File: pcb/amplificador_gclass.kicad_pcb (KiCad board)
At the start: 2 copper layers, 199.5 x 70.5 mm, 97 parts, among them CON1 AUDIO_IN, P1 +VA_GND, P10 2SC3281, P11 2SC3281, P12 2SA1302, P13 CONN_01X01, P14 CONN_01X01, P15 CONN_01X01, P16 CONN_01X01, P17 CONN_01X01, P18 CONN_01X01, P2 +VB_GND, P3 -VA_GND, P4 -VB_GND, P5 OUT, P6 CONN_01X01, P7 MJE350, P8 MJE340, P9 2SA1302, Q1 MPSA56_PNP_EBC, Q10 MPSA06_NPN_EBC, Q11 MPSA56_PNP_EBC, Q12 MPSA06_NPN_EBC, Q13 MPSA56_PNP_EBC, Q14 MPSA06_NPN_EBC, Q15 MPSA56_PNP_EBC, Q16 MPSA06_NPN_EBC, Q17 MJE340_NPN_ECB, Q18 MJE350_PNP_EBC, Q19 MJE340_NPN_ECB, Q2 MPSA56_PNP_EBC, Q20 MJE350_PNP_EBC, Q3 MPSA06_NPN_EBC, Q4 MPSA56_PNP_EBC, Q5 MPSA06_NPN_EBC, Q6 MPSA56_PNP_EBC, Q7 MPSA56_PNP_EBC, Q8 MPSA56_PNP_EBC, Q9 MPSA56_PNP_EBC

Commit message: cambios
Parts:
- added P21: CONN_01X03, pcb:bornera_grande, F.Cu at (26.1, 129.3)
- added P22: CONN_01X03, pcb:bornera_grande, F.Cu at (25.9, 164.4)
- added Q23: Q_NPN_BCE, pcb:transistor_salida, F.Cu at (35.5, 136.9)
- added Q24: Q_PNP_BCE, pcb:transistor_salida, F.Cu at (36.6, 171.9)
- moved R12 30.1 mm to (195.4, 100.8)
- moved C12 30.1 mm to (208.8, 40.9)
- moved C6 30.1 mm to (84.4, 49.6)
- moved CON1 30.1 mm to (41.0, 57.3)
- moved P7 30.1 mm to (128.9, 57.9)
- moved Q19 30.1 mm to (134.6, 41.8)
- moved R13 30.1 mm to (91.4, 56.0)
- moved R30 30.1 mm to (214.1, 58.6)
- moved C1 30.1 mm to (55.0, 66.8)
- moved C10 30.1 mm to (167.8, 56.9)
- moved C11 30.1 mm to (209.1, 94.2)
- moved C13 30.1 mm to (209.1, 53.2)
- moved C14 30.1 mm to (209.0, 81.8)
- moved C15 30.1 mm to (211.9, 73.4)
- moved C2 30.1 mm to (48.2, 84.4)
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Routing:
- net GND: track 492.1 -> 694.9 mm
- net Net-(Q7-Pad2): track 339.5 -> 309.0 mm
- net Net-(P22-Pad3): track 0.00 -> 11.4 mm
- net Net-(P22-Pad1): track 0.00 -> 11.3 mm
- net Net-(P22-Pad2): track 0.00 -> 10.7 mm
- net A1: track 0.00 -> 10.1 mm
- net Net-(P21-Pad1): track 0.00 -> 10.0 mm
- net Net-(P21-Pad2): track 0.00 -> 9.42 mm
- net FBACK: track 110.7 -> 108.6 mm
- net Net-(P9-Pad3): track 8.96 -> 6.94 mm
- removed copper zone on B.Cu, net GND
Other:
- board size 199.5 x 70.5 mm -> 210.9 x 154.2 mm

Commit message: pcb terminado
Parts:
- removed CON1: AUDIO_IN, Connect:BARREL_JACK
- removed the P1 at (219.2, 40.9)
- removed the P2 at (219.3, 53.2)
- removed the P3 at (219.1, 94.3)
- removed the P4 at (219.0, 81.8)
- added J1: Jack_3.5mm_5pin, pcb:jack_puto, F.Cu at (47.0, 51.4)
- added P5: +VA_GND, Pin_Headers:Pin_Header_Straight_1x02, F.Cu at (219.2, 40.9)
- added P6: +VB_GND, Pin_Headers:Pin_Header_Straight_1x02, F.Cu at (219.3, 53.2)
- added P7: -VA_GND, Pin_Headers:Pin_Header_Straight_1x02, F.Cu at (219.1, 94.3)
- added P8: -VB_GND, Pin_Headers:Pin_Header_Straight_1x02, F.Cu at (219.0, 81.8)
- moved P21 112.8 mm to (-15.8, 234.1)
- moved Q23 112.8 mm to (-6.40, 241.7)
- moved Q24 112.8 mm to (-5.35, 276.7)
- moved P22 112.8 mm to (-16.1, 269.1)
- renumbered P16 to P1, P14 to P10, P5 to P12, P6 to P13, P7 to P14, P8 to P15, P9 to P16, P10 to P17, P11 to P18, P12 to P19, P13 to P2, P15 to P3, P18 to P4, P17 to P9
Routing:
- net GND: track 694.9 -> 707.4 mm
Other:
- board size 210.9 x 154.2 mm -> 252.9 x 260.4 mm
- net class Default: trace_width 0.762 -> 1.27

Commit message: Arreglando PCB
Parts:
- removed P21, P22: CONN_01X03, pcb:bornera_grande
- removed Q23: Q_NPN_BCE, pcb:transistor_salida
- removed Q24: Q_PNP_BCE, pcb:transistor_salida
- removed REF** (x4): 1pin, Connect:1pin
- added R31: R, Resistors_ThroughHole:Resistor_Horizontal_RM10mm, F.Cu at (103.2, 41.5)
- added R32: R, Resistors_ThroughHole:Resistor_Horizontal_RM10mm, F.Cu at (88.6, 0.63)
- added R33: R, Resistors_ThroughHole:Resistor_Horizontal_RM10mm, F.Cu at (146.6, 8.28)
- added R34: R, Resistors_ThroughHole:Resistor_Horizontal_RM10mm, F.Cu at (42.4, -2.53)
- Q13: value MPSA56_PNP_EBC -> MPSA06_NPN_EBC
- Q14: value MPSA06_NPN_EBC -> MPSA56_PNP_EBC
- moved L1 174.1 mm to (61.1, -17.6), turned to 0 degrees
- moved R29 132.6 mm to (90.2, -8.01), turned to 0 degrees
- moved C15 125.6 mm to (119.4, -11.7)
- moved R30 122.2 mm to (105.6, 2.35), turned to 0 degrees
- moved R12 120.5 mm to (74.9, 97.5)
- moved P2 54.7 mm to (127.8, 3.57)
- moved R13 22.6 mm to (71.7, 45.0), turned to 270 degrees
- moved P4 20.9 mm to (83.9, 37.1)
- moved Q6 8.20 mm to (69.6, 50.3)
- moved Q4 7.03 mm to (77.2, 50.5)
- moved R3 5.89 mm to (48.6, 77.3)
- moved R1 4.02 mm to (46.7, 69.6)
- moved R7 1.88 mm to (78.3, 59.7)
- moved R4 1.88 mm to (64.7, 59.7)
- moved R9 0.63 mm to (63.6, 48.4)
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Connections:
- Q11 pad 1: +VA -> (no net)
- Q13 pad 1: +VA -> -VA
- Q13 pad 3: Net-(Q13-Pad2) -> Net-(Q13-Pad3)
- Q14 pad 1: -VA -> Net-(Q14-Pad1)
- Q14 pad 3: Net-(Q14-Pad2) -> Net-(D1-Pad1)
- Q15 pad 2: Net-(Q13-Pad2) -> Net-(Q14-Pad1)
- Q15 pad 3: Net-(D1-Pad1) -> Net-(Q14-Pad2)
- Q16 pad 1: -VA -> Net-(Q13-Pad2)
- Q16 pad 2: Net-(Q14-Pad2) -> Net-(Q13-Pad3)
- Q4 pad 1: +VA -> (no net)
- Q6 pad 2: Net-(Q4-Pad2) -> Net-(Q6-Pad2)
- Q9 pad 2: Net-(Q11-Pad2) -> Net-(Q9-Pad2)
- R13 pad 1: Net-(Q11-Pad2) -> +VA
- R13 pad 2: GND -> Net-(Q6-Pad2)
- R16 pad 1: Net-(Q13-Pad2) -> Net-(Q14-Pad2)
- R17 pad 1: Net-(Q14-Pad2) -> Net-(Q13-Pad3)
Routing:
- net GND: track 707.4 -> 396.5 mm, vias 2 -> 0
- net Net-(Q7-Pad2): track 309.0 -> 62.7 mm
- net +VA: track 226.9 -> 168.4 mm
- net -VA: track 309.8 -> 271.0 mm
- net FBACK: track 108.6 -> 146.8 mm
- net Net-(Q14-Pad2): track 34.4 -> 0.06 mm
- net Net-(Q13-Pad3): track 0.00 -> 25.6 mm
- net IN: track 39.8 -> 19.9 mm
- net Net-(Q4-Pad2): track 32.6 -> 12.8 mm
- net Net-(D1-Pad1): track 16.8 -> 3.45 mm
- net Net-(Q11-Pad2): track 13.0 -> 0.20 mm
- net Net-(C15-Pad1): track 12.1 -> 0.00 mm
- net Net-(P22-Pad3): track 11.4 -> 0.00 mm
- net Net-(P22-Pad1): track 11.3 -> 0.00 mm
- net Net-(P22-Pad2): track 10.7 -> 0.00 mm
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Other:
- board size 252.9 x 260.4 mm -> 199.5 x 73 mm

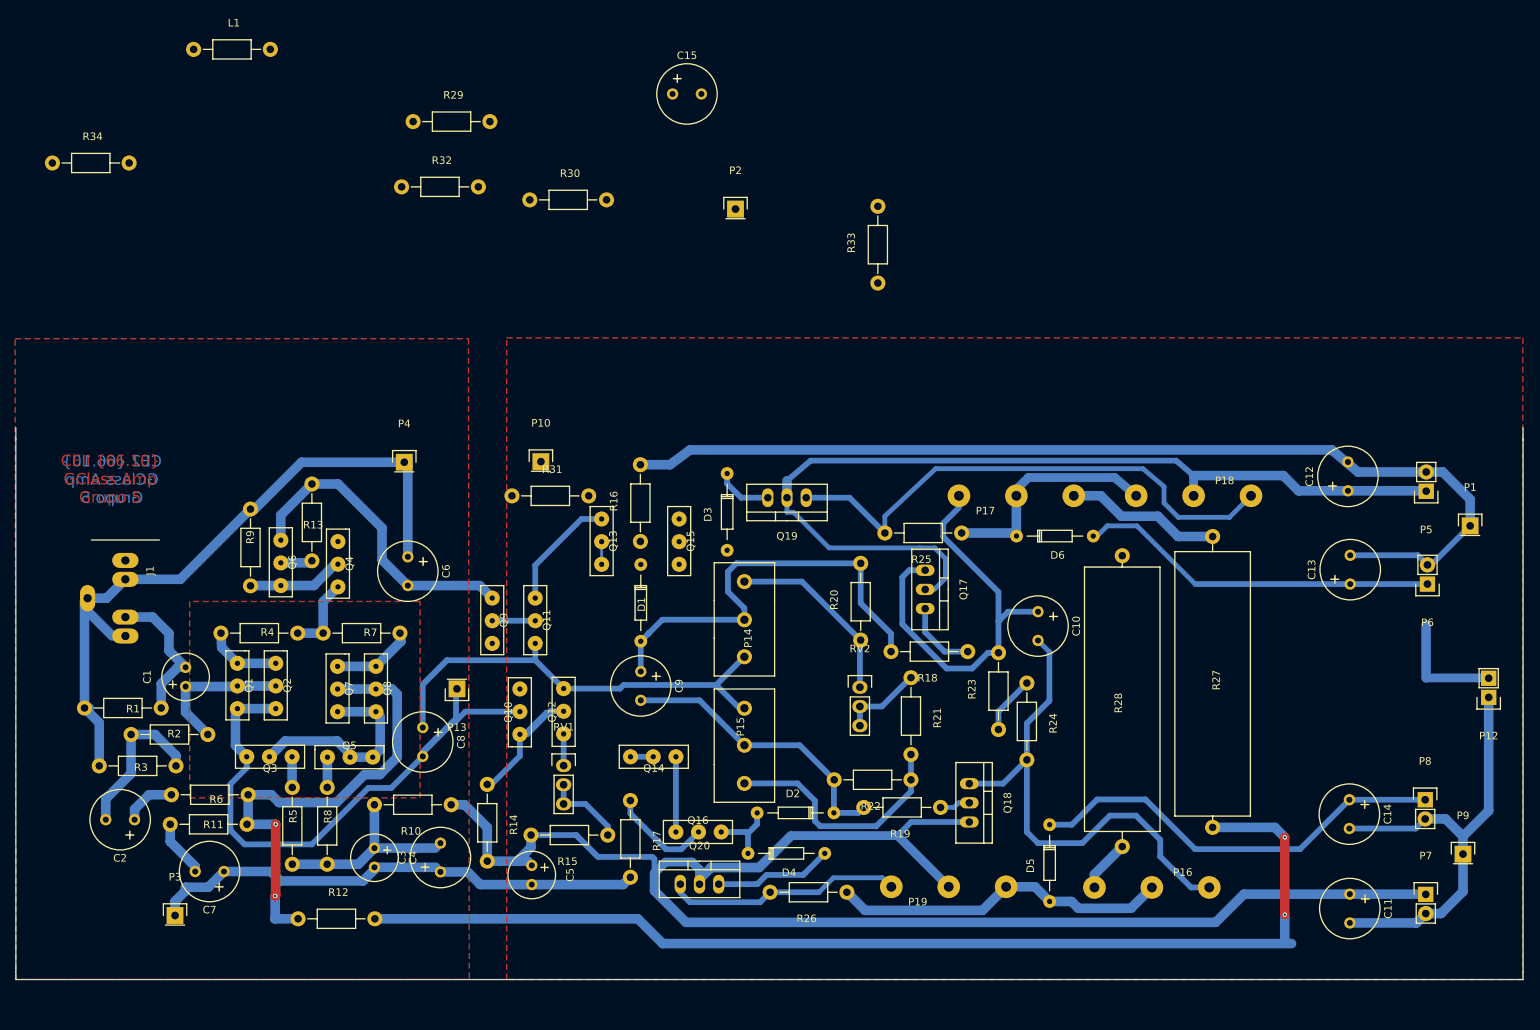
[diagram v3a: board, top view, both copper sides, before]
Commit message: Cambio las fuentes de corrientes por unas mas estables, agrando todas las pistas, agrego mini planos de tension para potencia, cambio pines de salida.
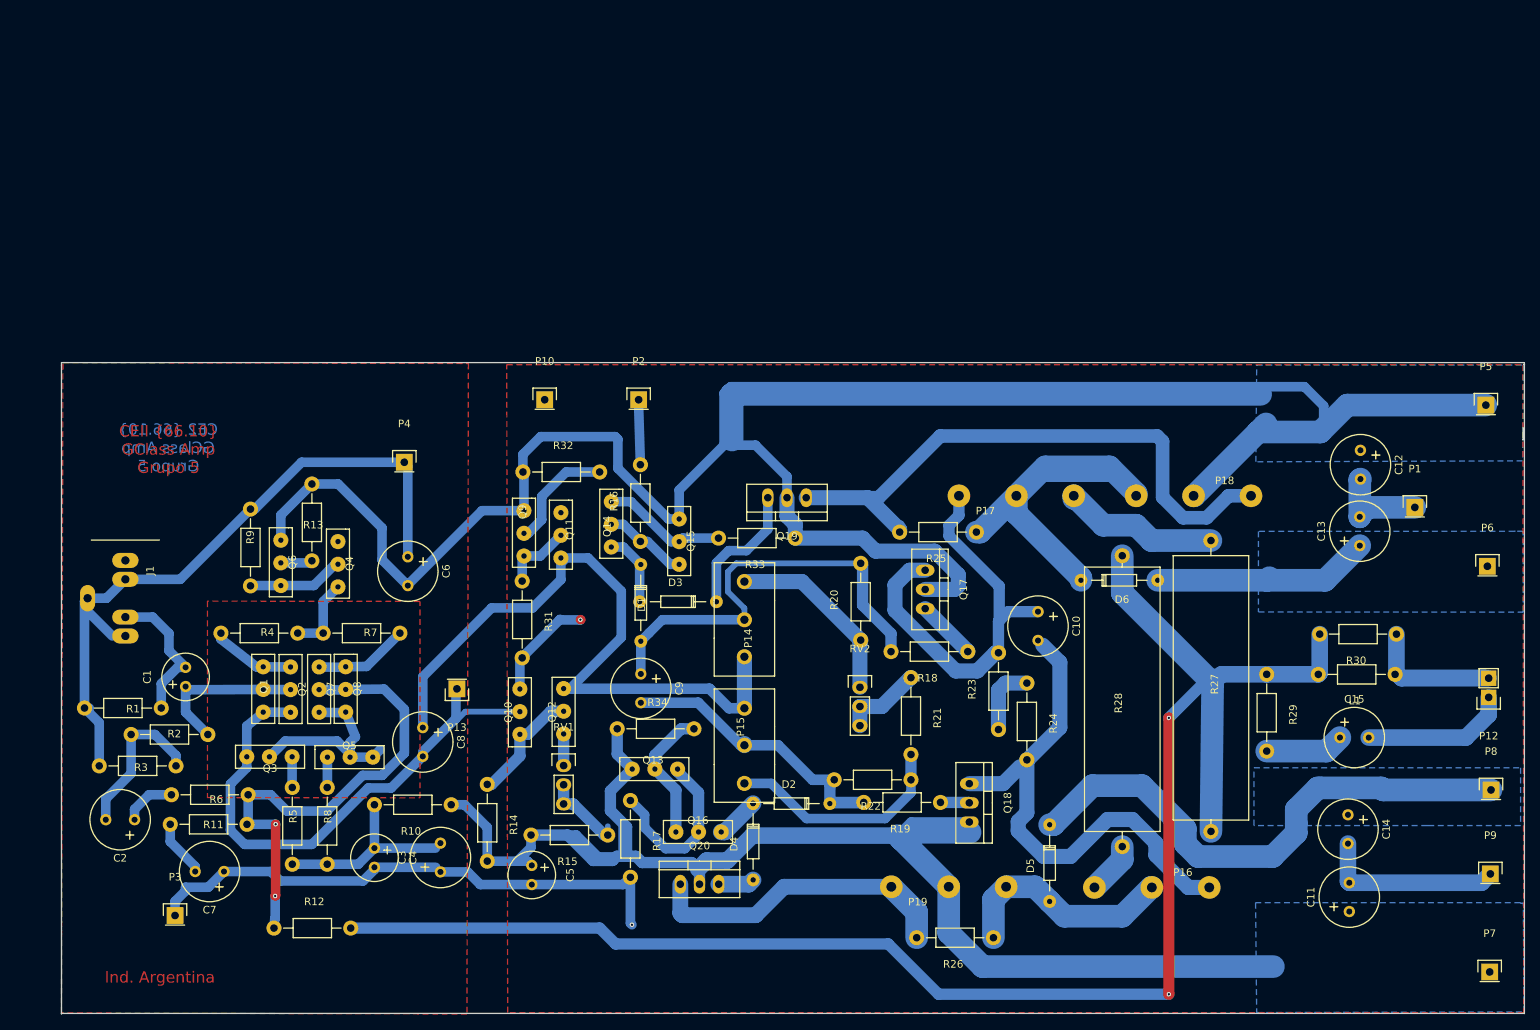
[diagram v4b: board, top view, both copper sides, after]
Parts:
- P5: value +VA_GND -> CONN_01X01; footprint Pin_Headers:Pin_Header_Straight_1x02 -> Pin_Headers:Pin_Header_Straight_1x01
- P6: value +VB_GND -> CONN_01X01; footprint Pin_Headers:Pin_Header_Straight_1x02 -> Pin_Headers:Pin_Header_Straight_1x01
- P7: value -VA_GND -> CONN_01X01; footprint Pin_Headers:Pin_Header_Straight_1x02 -> Pin_Headers:Pin_Header_Straight_1x01
- P8: value -VB_GND -> CONN_01X01; footprint Pin_Headers:Pin_Header_Straight_1x02 -> Pin_Headers:Pin_Header_Straight_1x01
- moved L1 170.3 mm to (210.0, 65.2), turned to 180 degrees
- moved R29 133.3 mm to (198.1, 70.2), turned to 270 degrees
- moved C15 122.7 mm to (207.8, 73.5)
- moved R30 119.3 mm to (210.2, 59.8), turned to 180 degrees
- moved R34 105.8 mm to (117.2, 72.4)
- moved R33 42.0 mm to (130.6, 47.1), turned to 180 degrees
- moved R32 41.0 mm to (104.7, 38.4)
- moved Q14 33.1 mm to (113.3, 45.2), turned to 270 degrees
- moved Q13 28.6 mm to (117.0, 75.7), turned to 0 degrees
- moved P2 28.3 mm to (114.9, 28.8)
- moved R26 20.3 mm to (156.8, 100.0)
- moved D3 17.0 mm to (125.2, 55.5), turned to 180 degrees
- moved R31 16.8 mm to (99.5, 57.9), turned to 270 degrees
- moved P5 13.9 mm to (227.1, 29.5), turned to 0 degrees
- moved P7 13.3 mm to (227.6, 104.5)
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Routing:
- net +VA: track 168.4 -> 381.3 mm
- net GND: track 396.5 -> 276.1 mm, vias 0 -> 2
- net FBACK: track 146.8 -> 257.5 mm
- net -VA: track 271.0 -> 236.7 mm
- net Net-(D6-Pad1): track 31.0 -> 60.0 mm
- net Net-(Q13-Pad2): track 3.00 -> 30.3 mm
- net Net-(C10-Pad2): track 67.6 -> 94.7 mm
- net OUT: track 15.3 -> 35.7 mm
- net Net-(R21-Pad1): track 19.2 -> 38.4 mm
- net Net-(P15-Pad3): track 49.3 -> 30.5 mm
- net Net-(P14-Pad3): track 49.8 -> 68.5 mm
- net +VB: track 48.0 -> 29.6 mm
- net -VB: track 56.5 -> 71.3 mm
- net Net-(D2-Pad2): track 18.9 -> 6.55 mm
- net Net-(C9-Pad2): track 62.1 -> 49.8 mm
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- added copper zone on B.Cu, net +VA
- added copper zone on B.Cu, net +VB
- added copper zone on B.Cu, net -VA
- added copper zone on B.Cu, net -VB
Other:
- board size 199.5 x 73 mm -> 193.7 x 86.2 mm
- net class Default: trace_width 1.27 -> 3
- board text added: "Ind. Argentina"

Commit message: Arreglo un par de cositas mas, creo que con esto ya etsamos.
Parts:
- moved P1 9.75 mm to (227.3, 41.7)
- moved P9 1.62 mm to (227.9, 90.0)
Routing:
- net GND: track 276.1 -> 295.7 mm
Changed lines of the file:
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@@
   (general
     (links 157)
-    (no_connects 0)
+    (no_connects 1)
     (area 38.4037 22.5251 250.202341 123.299469)
     (thickness 1.6)
     (drawings 17)
-    (tracks 663)
+    (tracks 669)
     (zones 0)
     (modules 97)
@@
   )
   (module Pin_Headers:Pin_Header_Straight_1x01 (layer F.Cu)
-    (at 217.6769 43.0535)
+    (at 227.3289 41.6565)
     (descr "Through hole pin header")
     (tags "pin header")
@@
   )
   (module Pin_Headers:Pin_Header_Straight_1x01 (layer F.Cu)
-    (at 227.6718 91.5675)
+    (at 227.9385 89.9673)
     (descr "Through hole pin header")
     (tags "pin header")
@@
   (segment (start 47.7576 78.2824) (end 47.7576 73.116) (width 1.27) (layer B.Cu) (net 4))
   (segment (start 44.4048 84.3936) (end 44.4048 81.6352) (width 1.27) (layer B.Cu) (net 4))
-  (segment (start 210.3871 44.30318) (end 210.3871 39.3959) (width 3) (layer B.Cu) (net 5))
+  (segment (start 210.3871 44.30318) (end 210.3871 39.3959) (width 3) (layer B.Cu) (net 5) (status C00000))
+  (segment (start 210.3871 39.3959) (end 210.476 39.307) (width 3) (layer B.Cu) (net 5) (status C00000))
+  (segment (start 209.0028 92.7359) (end 209.0028 87.7321) (width 3) (layer B.Cu) (net 5) (status C00000))
+  (segment (start 209.0028 87.7321) (end 208.825 87.5543) (width 3) (layer B.Cu) (net 5) (status C00000))
+  (segment (start 227.9385 89.9673) (end 209.3584 89.9673) (width 3) (layer B.Cu) (net 5) (status 400000))
+  (segment (start 209.3584 89.9673) (end 208.825 89.4339) (width 3) (layer B.Cu) (net 5))
+  (segment (start 227.3289 41.6565) (end 212.7747 41.6565) (width 3) (layer B.Cu) (net 5))
+  (segment (start 212.5588 41.8724) (end 210.3871 41.8724) (width 3) (layer B.Cu) (net 5))
+  (segment (start 212.7747 41.6565) (end 212.5588 41.8724) (width 3) (layer B.Cu) (net 5))
+  (segment (start 210.3871 44.30318) (end 210.3871 41.8724) (width 3) (layer B.Cu) (net 5))
+  (segment (start 210.3871 41.8724) (end 210.3871 39.3959) (width 3) (layer B.Cu) (net 5))
   (segment (start 210.3871 39.3959) (end 210.476 39.307) (width 3) (layer B.Cu) (net 5))
-  (segment (start 210.3871 44.30318) (end 210.5395 43.93742) (width 3) (layer B.Cu) (net 5) (status 10))
-  (segment (start 211.42342 43.0535) (end 217.6769 43.0535) (width 3) (layer B.Cu) (net 5))
-  (segment (start 210.5395 43.93742) (end 211.42342 43.0535) (width 3) (layer B.Cu) (net 5))
-  (segment (start 208.825 87.5543) (end 208.825 92.5581) (width 2.2) (layer B.Cu) (net 5))
+  (segment (start 208.825 87.5543) (end 208.825 89.4339) (width 2.2) (layer B.Cu) (net 5))
+  (segment (start 208.825 89.4339) (end 208.825 92.5581) (width 2.2) (layer B.Cu) (net 5))
   (segment (start 208.825 92.5581) (end 209.0028 92.7359) (width 2.2) (layer B.Cu) (net 5))
-  (segment (start 209.0028 92.7359) (end 226.5034 92.7359) (width 2.2) (layer B.Cu) (net 5))
-  (segment (start 226.5034 92.7359) (end 227.6718 91.5675) (width 2.2) (layer B.Cu) (net 5))
   (segment (start 113.8484 92.0136) (end 113.8484 98.0984) (width 1.27) (layer B.Cu) (net 5))
   (via (at 114.05 98.3) (size 0.6) (layers F.Cu B.Cu) (net 5))

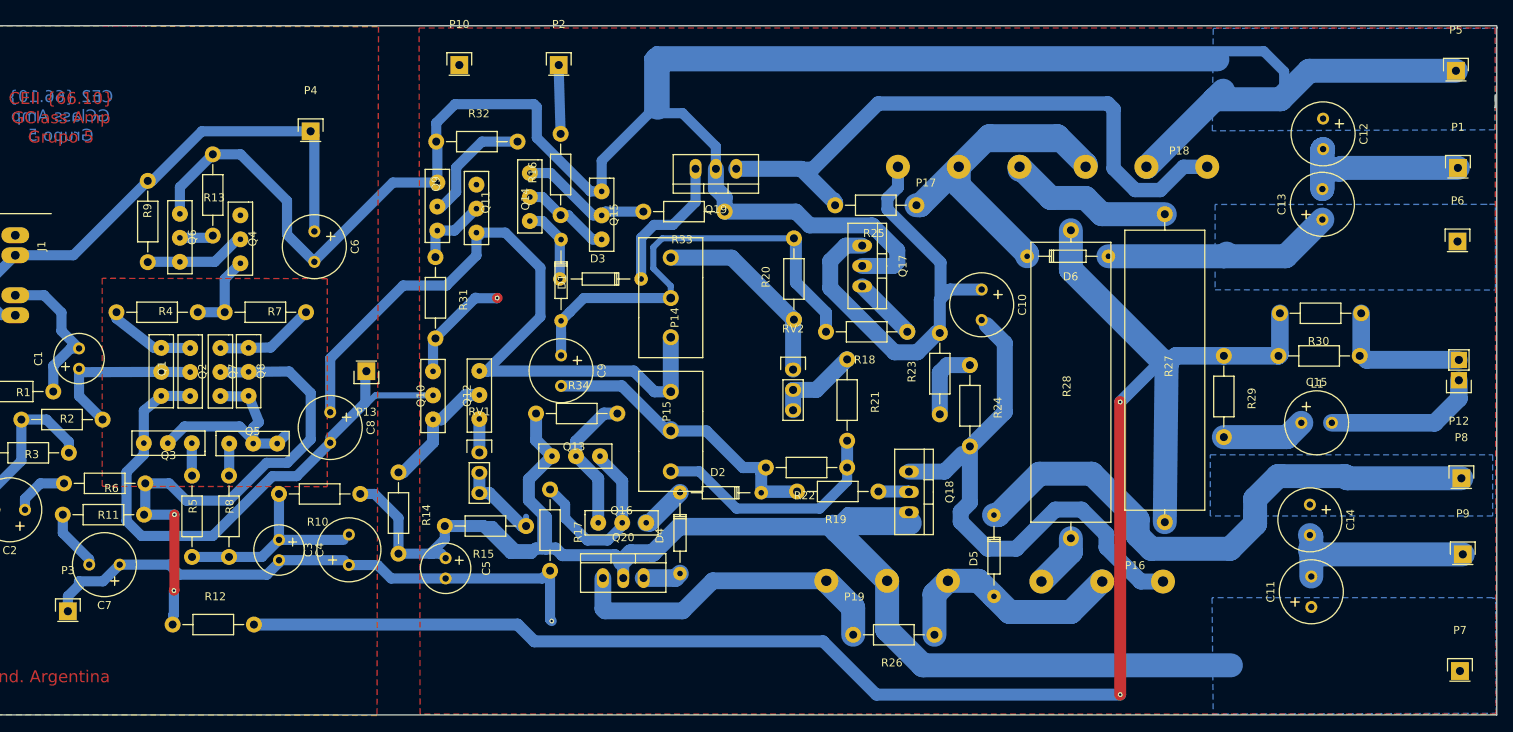
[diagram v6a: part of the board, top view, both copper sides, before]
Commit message: Agrando mucho mas las pistas, agrego pin de entrada, muevo diodo zener
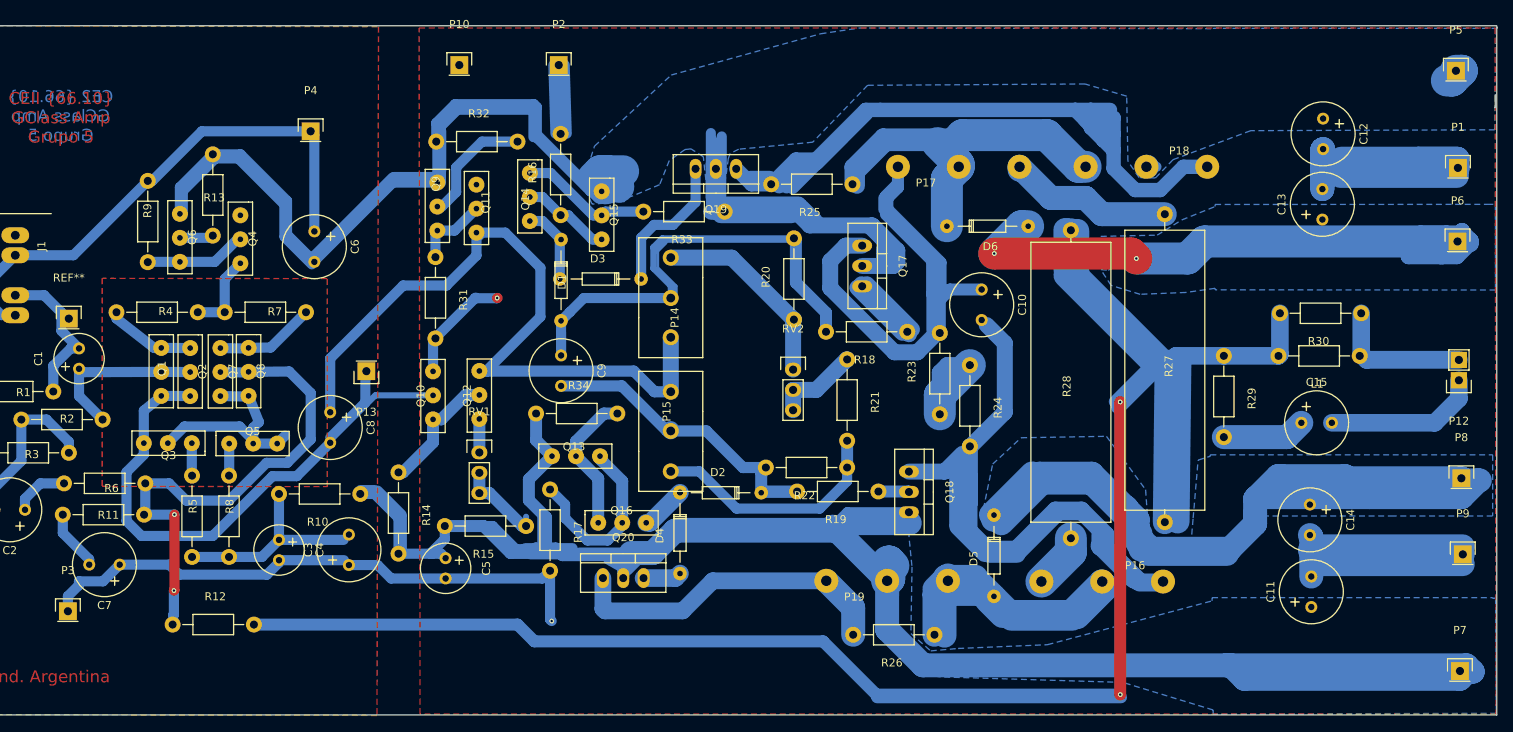
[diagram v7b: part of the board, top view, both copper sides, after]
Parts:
- added REF**: Pin_Header_Straight_1x01, Pin_Headers:Pin_Header_Straight_1x01, F.Cu at (53.7, 60.5)
- moved D6 10.7 mm to (163.4, 49.0)
- moved R25 8.41 mm to (146.6, 43.7)
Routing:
- net -VA: track 236.7 -> 352.3 mm
- net FBACK: track 257.5 -> 358.8 mm
- net +VA: track 381.3 -> 290.4 mm
- net GND: track 295.7 -> 384.1 mm
- net -VB: track 71.3 -> 159.2 mm
- net +VB: track 29.6 -> 94.9 mm, vias 0 -> 2
- net Net-(C10-Pad2): track 94.7 -> 154.3 mm
- net Net-(P18-Pad1): track 79.5 -> 114.1 mm
- net Net-(Q17-Pad3): track 16.0 -> 47.9 mm
- net Net-(D5-Pad2): track 37.3 -> 68.1 mm
- net Net-(C9-Pad1): track 109.4 -> 134.7 mm
- net Net-(C10-Pad1): track 67.7 -> 91.3 mm
- net (no net): track 0.00 -> 20.0 mm
- net Net-(D6-Pad1): track 60.0 -> 68.0 mm
- net Net-(R23-Pad1): track 17.6 -> 25.4 mm
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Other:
- net class Default: trace_width 3 -> 4
